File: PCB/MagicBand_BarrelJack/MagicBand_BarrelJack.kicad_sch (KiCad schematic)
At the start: 20 parts, among them J2 MFRC522_Module, J3 RF_TX_DFLIFE, J6 NeoPixel_Outer_16px, J7 NeoPixel_Inner_12px, J8 PWR_IN_BarrelJack_BareLeads, J9 ISP_AVR_2x3, Q1 AO3401A_PMOS_G-S-D, U1 ATmega328P-P, U2 MCP1700-3302, Y1 16MHz

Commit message: Swap C5/R1/R2 to SMD footprints (was left uncommitted from layout work)
Footprint-only change, no wiring/net impact: C5 (bulk cap) and R1/R2
(reset pullup, gate resistor) were THT parts inconsistent with the rest
of the board's SMD passives, swapped during PCB layout to help hit the
40x40mm target. This commit was missed in the layout commit itself --
caught by checking git status after, not assumed clean. ERC re-confirmed
clean (0 errors, 209 warnings, unchanged).

Co-Authored-By: Claude Sonnet 5 <noreply@anthropic.com>
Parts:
- C5: footprint Capacitor_THT:C_Disc_D5.0mm_W2.5mm_P5.00mm -> Capacitor_SMD:C_0805_2012Metric
- R1, R2: footprint Resistor_THT:R_Axial_DIN0207_L6.3mm_D2.5mm_P10.16mm_Horizontal -> Resistor_SMD:R_0603_1608Metric
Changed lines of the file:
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@@
 			(effects (font (size 1.27 1.27)))
 		)
-		(property "Footprint" "Capacitor_THT:C_Disc_D5.0mm_W2.5mm_P5.00mm"
+		(property "Footprint" "Capacitor_SMD:C_0805_2012Metric"
 			(at 170 100 0)
 			(effects (font (size 1.27 1.27)) (hide yes))
@@
 			(effects (font (size 1.27 1.27)))
 		)
-		(property "Footprint" "Resistor_THT:R_Axial_DIN0207_L6.3mm_D2.5mm_P10.16mm_Horizontal"
+		(property "Footprint" "Resistor_SMD:R_0603_1608Metric"
 			(at 140 145 0)
 			(effects (font (size 1.27 1.27)) (hide yes))
@@
 			(effects (font (size 1.27 1.27)))
 		)
-		(property "Footprint" "Resistor_THT:R_Axial_DIN0207_L6.3mm_D2.5mm_P10.16mm_Horizontal"
+		(property "Footprint" "Resistor_SMD:R_0603_1608Metric"
 			(at 220 181.27 0)
 			(effects (font (size 1.27 1.27)) (hide yes))

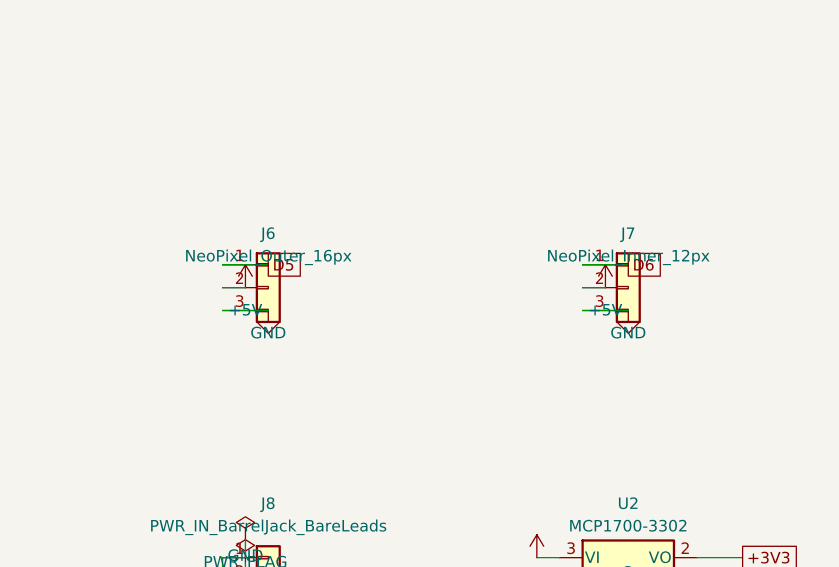
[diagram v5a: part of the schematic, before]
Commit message: Remove J7 (inner NeoPixel ring) from schematic and PCB, verified clean
Completes the LED-strip scope change deferred at the end of the last
session. Removed J7 (component, D6 wiring, its dedicated power
symbols) from the schematic, its footprint plus 2 dangling track
stubs from the PCB, and renamed J6's value to NeoPixel_LED_Strip
(count-agnostic, pending the ordered strip).

Verified via kicad-cli, not assumed: ERC 0 errors (129 warnings, down
from 209, all pre-existing cosmetic), DRC 0 unconnected pads / 0
footprint errors (188 violations, down from 202). Confirmed side
benefit: npth_inside_courtyard dropped 3->2, the MH3/J7 courtyard
conflict is gone. Regenerated all tracked exports (ERC/DRC reports,
schematic PDF, board SVGs) to match.

Co-Authored-By: Claude Sonnet 5 <noreply@anthropic.com>
Claude-Session: https://claude.ai/code/session_01WRfsGJdmccHFit2MbdKbSy
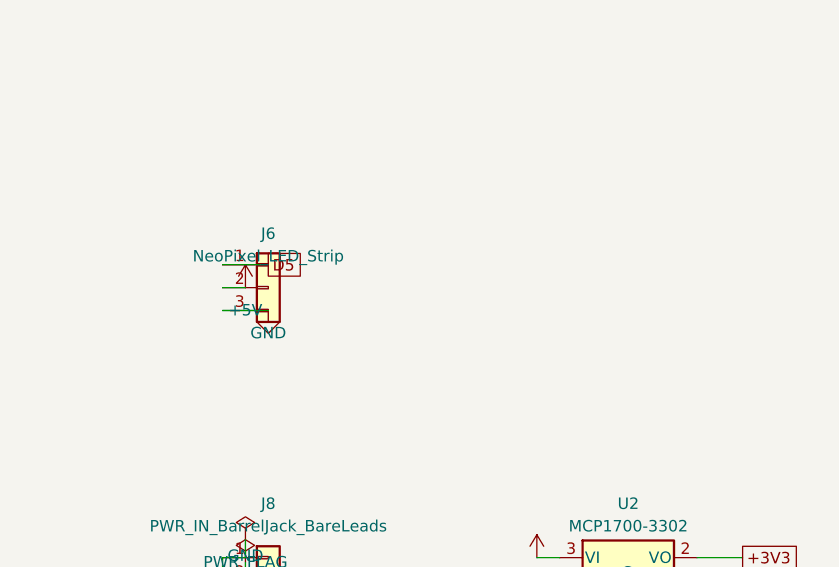
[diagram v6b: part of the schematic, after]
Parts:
- removed J7: NeoPixel_Inner_12px, Connector_JST:JST_PH_B3B-PH-K_1x03_P2.00mm_Vertical, symbol Connector_Generic:Conn_01x03
- J6: value NeoPixel_Outer_16px -> NeoPixel_LED_Strip
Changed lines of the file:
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@@
 			(effects (font (size 1.27 1.27)))
 		)
-		(property "Value" "NeoPixel_Outer_16px"
+		(property "Value" "NeoPixel_LED_Strip"
 			(at 250 96.5 0)
 			(effects (font (size 1.27 1.27)))
@@
 					(unit 1)
 				)
-			)
-		)
-	)
-	(symbol
-		(lib_id "Connector_Generic:Conn_01x03")
-		(at 290 100 0)
-		(unit 1)
-		(exclude_from_sim no)
-		(in_bom yes)
-		(on_board yes)
-		(dnp no)
-		(property "Reference" "J7"
-			(at 290 94 0)
-			(effects (font (size 1.27 1.27)))
-		)
-		(property "Value" "NeoPixel_Inner_12px"
-			(at 290 96.5 0)
-			(effects (font (size 1.27 1.27)))
-		)
-		(property "Footprint" "Connector_JST:JST_PH_B3B-PH-K_1x03_P2.00mm_Vertical"
-			(at 290 100 0)
-			(effects (font (size 1.27 1.27)) (hide yes))
-		)
-		(property "Datasheet" ""
-			(at 290 100 0)
-			(effects (font (size 1.27 1.27)) (hide yes))
-		)
-		(pin "1")
-		(pin "2")
-		(pin "3")
-		(instances
-			(project "MagicBand_BarrelJack"
-				(path "/bcfef247-dfd6-4ae3-b42f-2bc22ccfcf8a"
-					(reference "J7")
-					(unit 1)
-				)
-			)
-		)
-	)
-	(wire
-		(pts (xy 284.92 97.46) (xy 290.0 97.46))
-		(stroke (width 0) (type default))
-	)
-	(global_label "D6"
-		(shape passive)
-		(at 290.0 97.46 0)
-		(fields_autoplaced yes)
-		(effects (font (size 1.27 1.27)) (justify left))
-	)
-	(wire
-		(pts (xy 284.92 100.0) (xy 287.46 100.0))
-		(stroke (width 0) (type default))
-	)
-	(symbol
-		(lib_id "power:+5V")
-		(at 287.46 100.0 0)
-		(unit 1)
-		(exclude_from_sim no)
-		(in_bom yes)
-		(on_board yes)
-		(dnp no)
-		(property "Reference" "#PWR1032"
-			(at 287.46 96.5 0)
-			(effects (font (size 1.27 1.27)) (hide yes))
-		)
-		(property "Value" "+5V"
-			(at 287.46 102.5 0)
-			(effects (font (size 1.27 1.27)))
-		)
-		(property "Footprint" ""
-			(at 287.46 100.0 0)
-			(effects (font (size 1.27 1.27)) (hide yes))
-		)
-		(property "Datasheet" ""
-			(at 287.46 100.0 0)
-			(effects (font (size 1.27 1.27)) (hide yes))
-		)
-		(pin "1")
-		(instances
-			(project "MagicBand_BarrelJack"
-				(path "/bcfef247-dfd6-4ae3-b42f-2bc22ccfcf8a"
-					(reference "#PWR1032")
-					(unit 1)
-				)
-			)
-		)
-	)
-	(wire
-		(pts (xy 284.92 102.54) (xy 290.0 102.54))
-		(stroke (width 0) (type default))
-	)
-		(symbol
-		(lib_id "power:GND")
-		(at 290.0 102.54 0)
-		(unit 1)
-		(exclude_from_sim no)
-		(in_bom yes)
-		(on_board yes)
-		(dnp no)
-		(property "Reference" "#PWRJ7G1"
-			(at 290.0 99.04 0)
-			(effects (font (size 1.27 1.27)) (hide yes))
-		)
-		(property "Value" "GND"
-			(at 290.0 105.04 0)
-			(effects (font (size 1.27 1.27)))
-		)
-		(property "Footprint" ""
-			(at 290.0 102.54 0)
-			(effects (font (size 1.27 1.27)) (hide yes))
-		)
-		(property "Datasheet" ""
-			(at 290.0 102.54 0)
-			(effects (font (size 1.27 1.27)) (hide yes))
-		)
-		(pin "1")
-		(instances
-			(project "MagicBand_BarrelJack"
-				(path "/bcfef247-dfd6-4ae3-b42f-2bc22ccfcf8a"
-					(reference "#PWRJ7G1")
-					(unit 1)
-				)
